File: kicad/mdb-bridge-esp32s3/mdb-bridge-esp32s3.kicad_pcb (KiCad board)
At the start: 2 copper layers, 39 x 40 mm, 53 parts, among them J1 MDB_Connector, J2 USB_C_Receptacle_USB2.0_16P, J4 Conn_Coaxial, J8 Conn_01x04_Pin, J9 MDB_Connector, Q8 MMBT3904, SW1 SW_Push, U1 TLP785, U3 ESP32-S3FH4R2, U4 TLP785, U5 LM2594HVM-3.3, U7 MT3608, Y1 Crystal_GND24

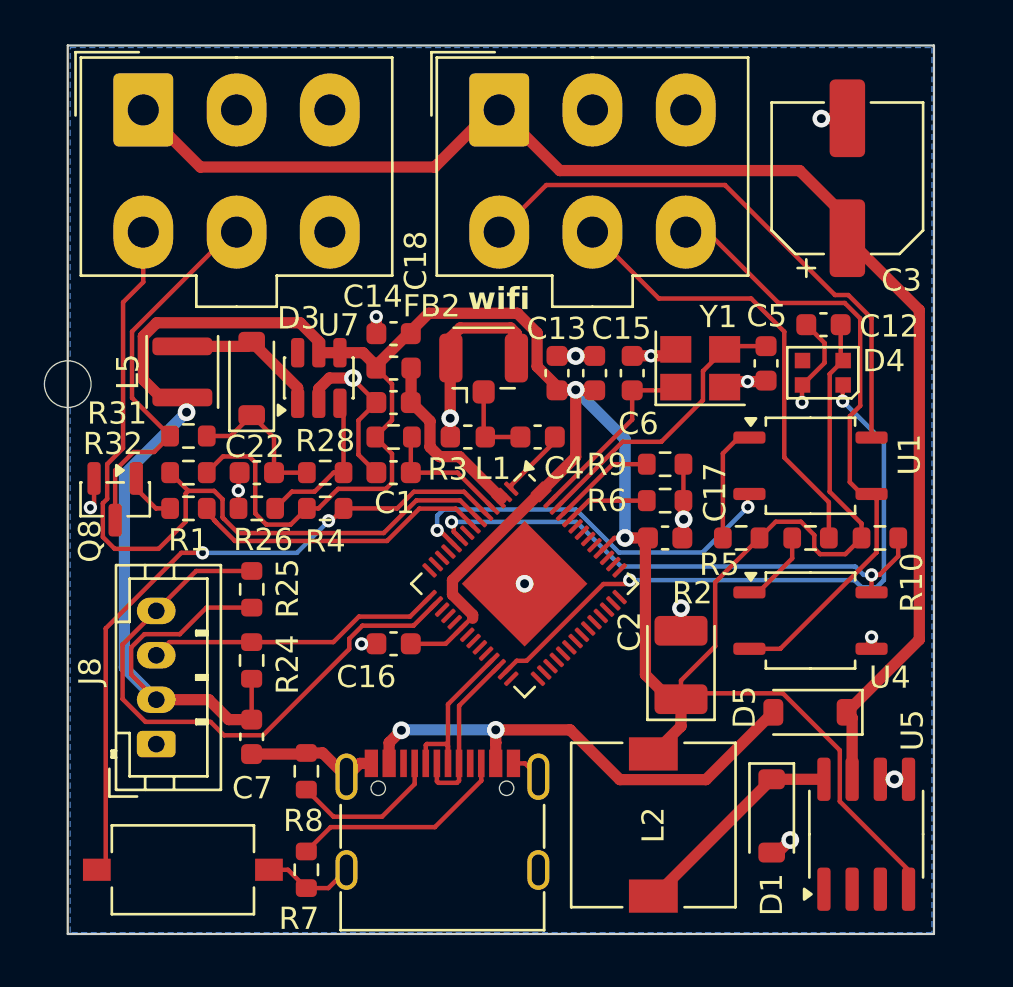
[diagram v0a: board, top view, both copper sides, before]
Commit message: fix(hardware): update LCSC# and values in mdb-bridge-esp32s3 schematic
- C3: Value "?" → "1uF", LCSC# → C696901 (AP2112K-3.3 input cap)
- C1, C2, C15: LCSC# C6119849 → C696901 (discontinued → active 1uF 16V X5R 0603)
- C32: Value "220uF" → "100uF", LCSC# → C90975 (LM2594HVM-5V output, 10V CASE-B derating)

Co-Authored-By: Claude Sonnet 4.6 <noreply@anthropic.com>
Claude-Session: https://claude.ai/code/session_01Qh1XTvg8Um6L2D2gYWdT7R
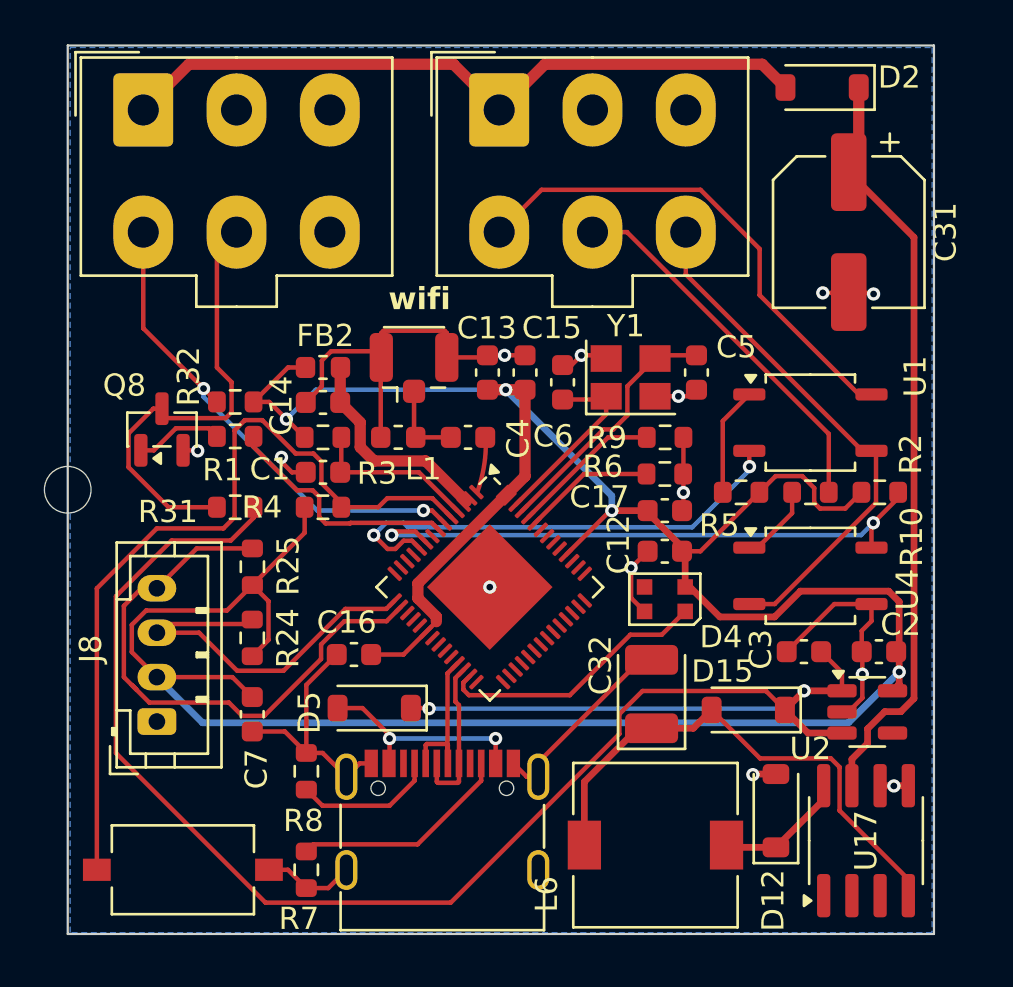
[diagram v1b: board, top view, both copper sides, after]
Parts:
- removed C18, C22: 22pF, Capacitor_SMD:C_0603_1608Metric
- removed D1, D3: D_Schottky, Diode_SMD:D_SOD-123
- removed L2: 100uH, Inductor_SMD:L_7.3x7.3_H3.5
- removed L5: 4.7uF, Inductor_SMD:L_APV_ANR3015
- removed R26: 15k, Resistor_SMD:R_0603_1608Metric
- removed R28: 110k, Resistor_SMD:R_0603_1608Metric
- removed U5: LM2594HVM-3.3, Package_SO:SOIC-8_3.9x4.9mm_P1.27mm
- removed U7: MT3608, Package_TO_SOT_SMD:SOT-23-6
- added C31: 100uF, Capacitor_SMD:CP_Elec_6.3x5.8, F.Cu at (203.7, 91.5)
- added C32: 100uF, Capacitor_Tantalum_SMD:CP_EIA-3528-21_Kemet-B, F.Cu at (194.8, 112.3)
- added D12: D_Schottky, Diode_SMD:D_SOD-123, F.Cu at (200.4, 117.5)
- added D15: D_Schottky, Diode_SMD:D_SOD-123, F.Cu at (199.1, 113.0)
- added D2: D_Schottky, Diode_SMD:D_SOD-123, F.Cu at (202.5, 85.0)
- added L6: 100uH, Inductor_SMD:L_7.3x7.3_H3.5, F.Cu at (195.0, 119.1)
- added U17: LM2594HVM-5.0, Package_SO:SOIC-8_3.9x4.9mm_P1.27mm, F.Cu at (204.4, 118.9)
- added U2: AP2112K-3.3, Package_TO_SOT_SMD:SOT-23-5, F.Cu at (204.5, 113.1)
- C2: value 220uF -> 1uF; footprint Capacitor_Tantalum_SMD:CP_EIA-3528-21_Kemet-B -> Capacitor_SMD:C_0603_1608Metric
- C3: value 100uF -> 1uF; footprint Capacitor_SMD:CP_Elec_6.3x5.8 -> Capacitor_SMD:C_0603_1608Metric
- C4: value 1.8pf -> 1.8pF
- FB2: value FerriteBead_Small -> FerriteBead
- L1: value 2.4nh -> 2.4nH
- R2, R5: value 470ohm -> 470R
- R24, R25, R31: value 4K7 -> 4.7k
- Y1: value Crystal_GND24 -> 40MHz
- moved C3 21.4 mm to (201.6, 110.4), turned to 0 degrees
- moved D5 19.6 mm to (182.3, 112.9)
- moved C12 12.5 mm to (195.4, 105.9)
- moved D4 12.4 mm to (195.4, 108.0)
- moved C2 8.93 mm to (205.0, 110.4), turned to 0 degrees
- moved H1 4.76 mm to (168.5, 103.1)
- moved R1 3.87 mm to (176.0, 100.7)
- moved R31 3.84 mm to (176.0, 103.9)
- moved R32 3.82 mm to (176.0, 99.1)
- moved Q8 3.78 mm to (172.7, 100.4), turned to 90 degrees
- moved FB2 3.18 mm to (180.0, 97.6)
- moved R3 3.18 mm to (180.0, 100.7)
- moved C1 3.18 mm to (180.0, 102.3)
- moved C14 3.18 mm to (180.0, 99.2)
- moved C5 3.16 mm to (196.8, 97.8)
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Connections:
- C2 pad 1: +3V3 -> GND
- C2 pad 2: GND -> +3V3
- C3 pad 1: /vin -> GND
- C3 pad 2: GND -> +5V
- D5 pad 1: /vin -> +5V
- J1 pad 1: /vin -> /mdb_24v
- J9 pad 1: /vin -> /mdb_24v
- U3 pad 11: /io6 -> unconnected-(U3-GPIO6/ADC1_CH5-Pad11)
- U3 pad 12: /io7 -> unconnected-(U3-GPIO7/ADC1_CH6-Pad12)
- U3 pad 13: /io8 -> unconnected-(U3-GPIO8/ADC1_CH7-Pad13)
- U3 pad 14: /io9 -> unconnected-(U3-GPIO9/ADC1_CH8-Pad14)
- U3 pad 17: /io12 -> unconnected-(U3-GPIO12/ADC2_CH1-Pad17)
- U3 pad 18: /io13 -> unconnected-(U3-GPIO13/ADC2_CH2-Pad18)
- U3 pad 19: /io14 -> unconnected-(U3-GPIO14/ADC2_CH3-Pad19)
- U3 pad 23: /io17 -> unconnected-(U3-GPIO17/ADC2_CH6-Pad23)
- U3 pad 24: /io18 -> unconnected-(U3-GPIO18/ADC2_CH7-Pad24)
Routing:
- net +5V: track 6.90 -> 79.1 mm, vias 0 -> 2
- net /mdb_24v: track 0.00 -> 31.9 mm
- net /vin: track 64.4 -> 34.4 mm
- net Net-(D15-A): track 0.00 -> 23.8 mm
- net +3V3: track 157.4 -> 133.8 mm, vias 3 -> 4
- net GND: track 51.1 -> 70.1 mm, vias 17 -> 13
- net /io21: track 28.6 -> 12.4 mm, vias 2 -> 0
- net /io1: track 36.9 -> 22.6 mm, vias 0 -> 2
- net Net-(D5-A): track 22.2 -> 10.0 mm
- net Net-(D1-K): track 9.86 -> 0.00 mm
- net Net-(U7-FB): track 6.94 -> 0.00 mm
- net Net-(D3-A): track 6.83 -> 0.00 mm
- net Net-(D12-K): track 0.00 -> 5.94 mm
- net /boot: track 31.1 -> 36.9 mm, vias 2 -> 0
- net /mdb_communications_common: track 28.5 -> 23.6 mm
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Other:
- board text added: "mdb-bridge-esp32s3"
- board text removed: "mdb-dual-esp32s3"
